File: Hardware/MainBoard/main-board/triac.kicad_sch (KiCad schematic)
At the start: 14 parts, among them J4 Conn_01x03, J5 1366005, U2 DS18B20+, U3 MOC3083S-TA1

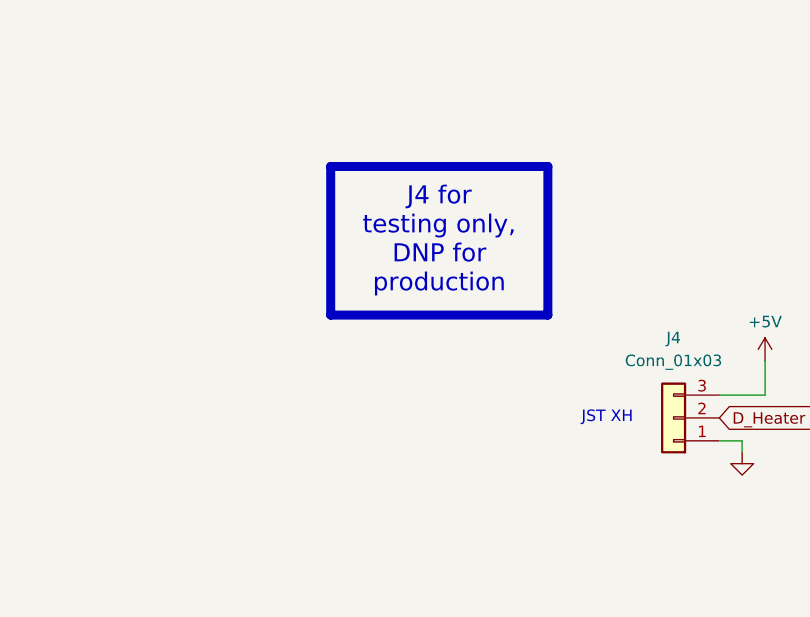
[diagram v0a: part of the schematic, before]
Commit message: add details, need to change TC amp gain for different voltage and temperature
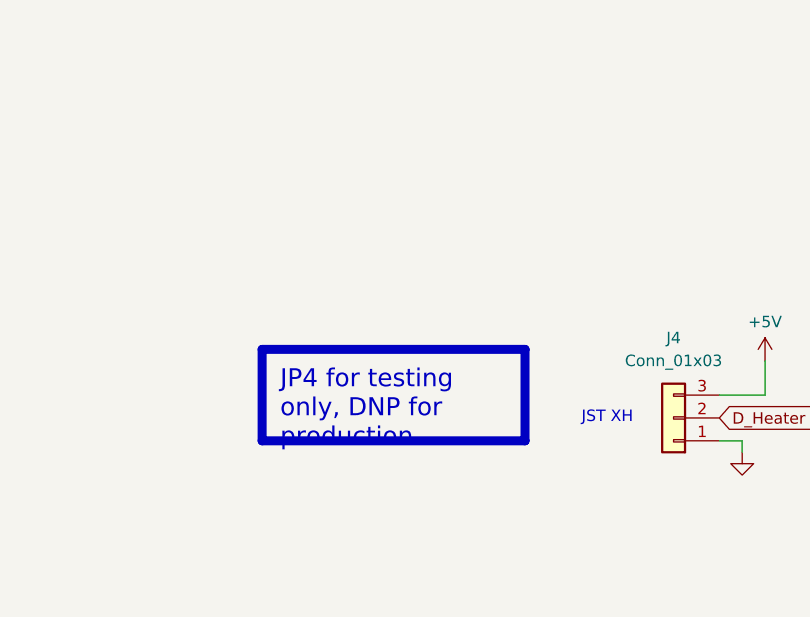
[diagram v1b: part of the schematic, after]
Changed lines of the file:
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@@
+		)
+	)
+	(text_box "JP4 for testing only, DNP for production"
+		(exclude_from_sim no)
+		(at 54.61 106.68 0)
+		(size 29.21 10.16)
+		(margins 2 2 2 2)
+		(stroke
+			(width 1)
+			(type solid)
+			(color 255 165 0 1)
+		)
+		(fill
+			(type none)
+		)
+		(effects
+			(font
+				(face "Arial")
+				(size 2 2)
+				(color 0 0 0 1)
+			)
+			(justify left top)
 		)
 	)
@@
 		)
 	)
-	(text_box "J4 for testing only, DNP for production"
-		(exclude_from_sim no)
-		(at 62.23 86.36 0)
-		(size 24.13 16.51)
-		(margins 2 2 2 2)
-		(stroke
-			(width 1)
-			(type solid)
-			(color 200 200 200 1)
-		)
-		(fill
-			(type none)
-		)
-		(effects
-			(font
-				(face "Arial")
-				(size 2 2)
-				(color 0 0 0 1)
-			)
-			(justify top)
-		)
-	)

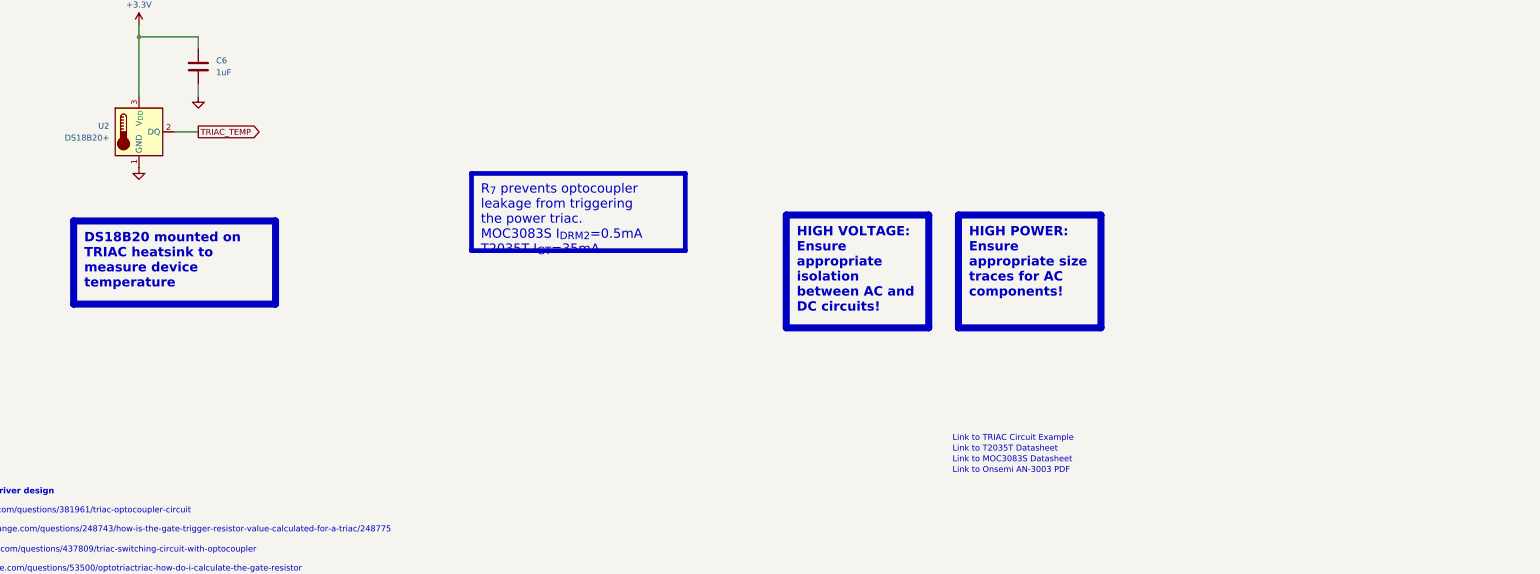
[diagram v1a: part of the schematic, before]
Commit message: add heatsink mounting holes, change a few footprints, clean up schematic
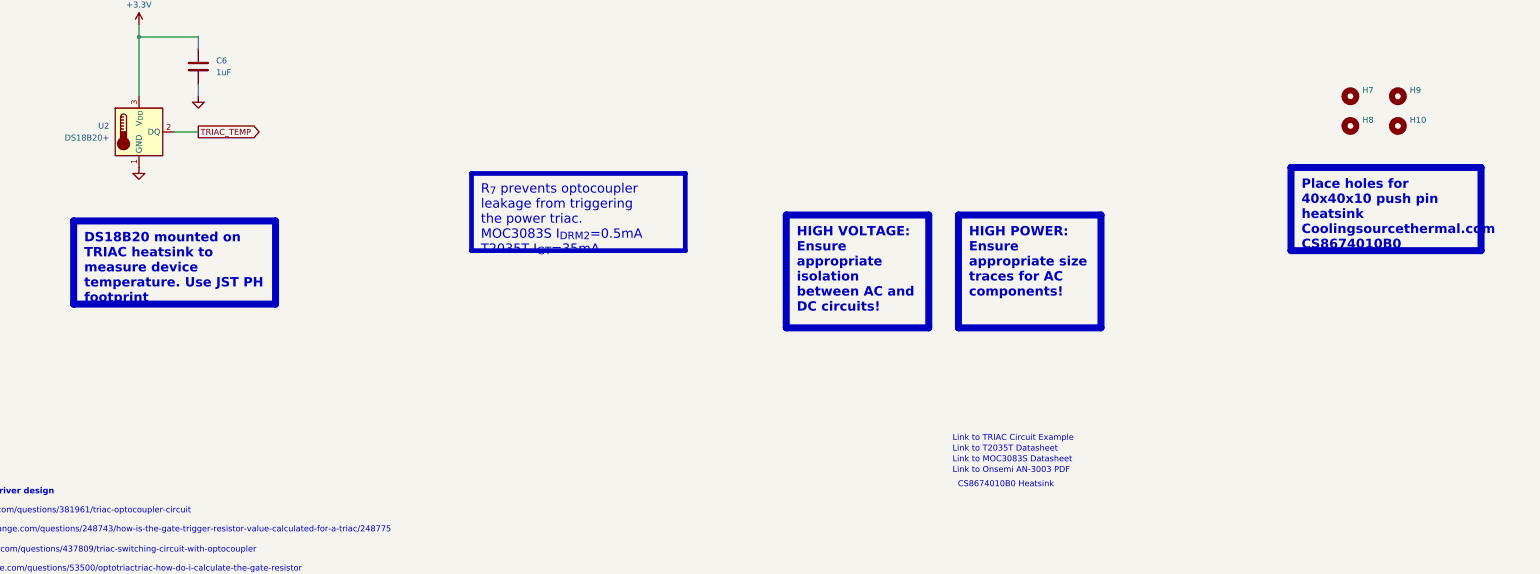
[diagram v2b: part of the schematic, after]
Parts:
- added H10, H7, H8, H9: MountingHole, MountingHole:MountingHole_3mm, symbol Mechanical:MountingHole
- U2: footprint Package_TO_SOT_THT:TO-92_Inline -> Connector_JST:JST_PH_B3B-PH-K_1x03_P2.00mm_Vertical
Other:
- note added: "CS8674010B0 Heatsink"

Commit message: Finish board layout
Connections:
- net L1: now also J5.3 (Pin_3); no longer J5.1 (Pin_1)
- net L1_HEATER: now also J5.1 (Pin_1); no longer J5.3 (Pin_3)
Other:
- moved on the sheet: J5
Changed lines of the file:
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@@
 	(symbol
 		(lib_id "Connector_Generic:Conn_01x03")
-		(at 303.53 104.14 270)
-		(mirror x)
+		(at 303.53 104.14 90)
 		(unit 1)
 		(exclude_from_sim no)
@@
 		(dnp no)
 		(property "Reference" "J5"
-			(at 298.45 102.8699 90)
+			(at 308.61 102.8699 90)
 			(effects
 				(font
@@
 		)
 		(property "Value" "1366005"
-			(at 298.45 105.4099 90)
+			(at 308.61 105.4099 90)
 			(effects
 				(font
